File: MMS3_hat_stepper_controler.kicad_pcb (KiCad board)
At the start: 4 copper layers, 100 x 50 mm, 98 parts, among them J1 Chainbus in, J2 Chainbus Out, J3 Conn_01x04_Pin, J4 AMASS XT60 Male, J5 AMASS XT60 Female, J6 Encoder connector, J7 Motor connector, J8 Conn_01x03_Pin, SW1 SW_DIP_x04, U1 SN74CB3Q3384APW, U2 M24C64, U3 TMC5130A-TA, U4 AMS1117, U5 LM2596HVS-ADJRG

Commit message: generated production files
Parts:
- moved H7 9.00 mm to (88.0, 136.8)
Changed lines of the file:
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@@
 	(footprint "PCM_JLCPCB:Hole_Tooling_JLCPCB"
 		(layer "F.Cu")
-		(at 79 137)
+		(at 88 136.828427)
 		(property "Reference" "H7"
 			(at 0 -0.5 0)
@@
 			(polygon
 				(pts
-					(xy 78 136) (xy 80 136) (xy 80 138) (xy 78 138)
+					(xy 87 135.828427) (xy 89 135.828427) (xy 89 137.828427) (xy 87 137.828427)
 				)
 			)

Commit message: added version number
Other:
- board text added: "Version 1.0 Made by Wojciech Szafrański"
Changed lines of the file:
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@@
+		)
+	)
+	(gr_text "Version 1.0\nMade by\nWojciech Szafrański"
+		(at 102 131 -0)
+		(layer "B.SilkS")
+		(effects
+			(font
+				(size 1 1)
+				(thickness 0.2)
+				(bold yes)
+			)
+			(justify mirror)
 		)
 	)

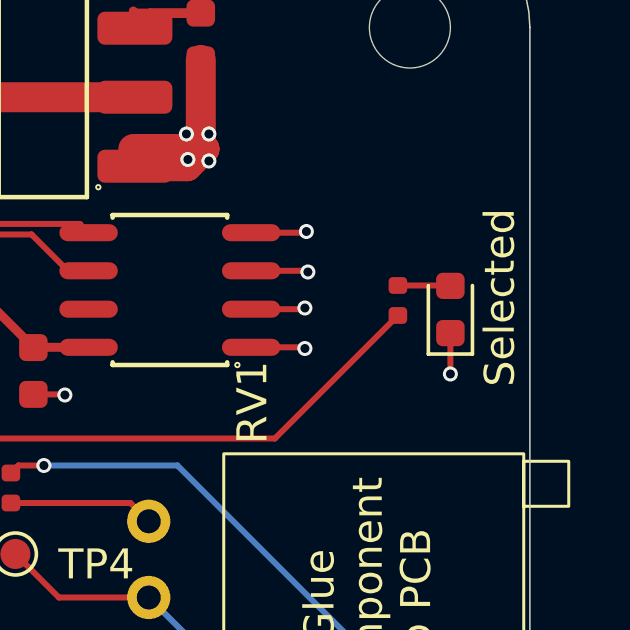
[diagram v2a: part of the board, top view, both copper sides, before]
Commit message: changed diode to JLCMANUFACTURING
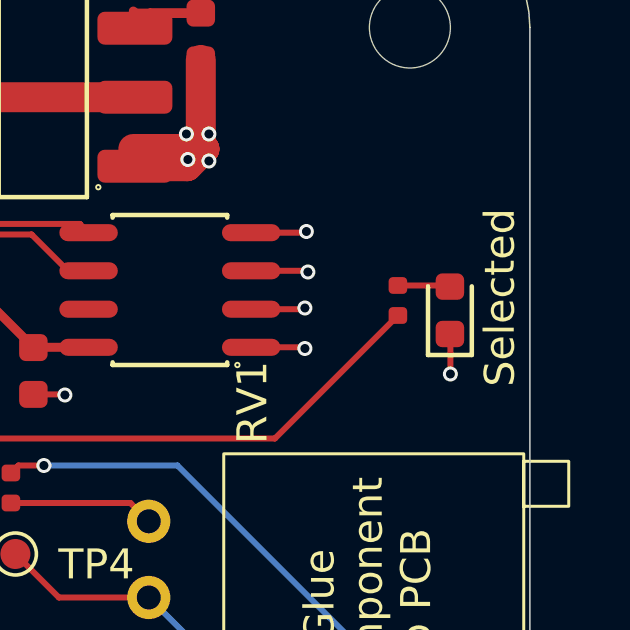
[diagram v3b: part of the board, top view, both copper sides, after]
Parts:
- removed D1: LED, LED_SMD:LED_0603_1608Metric
- added D7: Red, PCM_JLCPCB:D_0603, F.Cu at (175.3, 101.4)

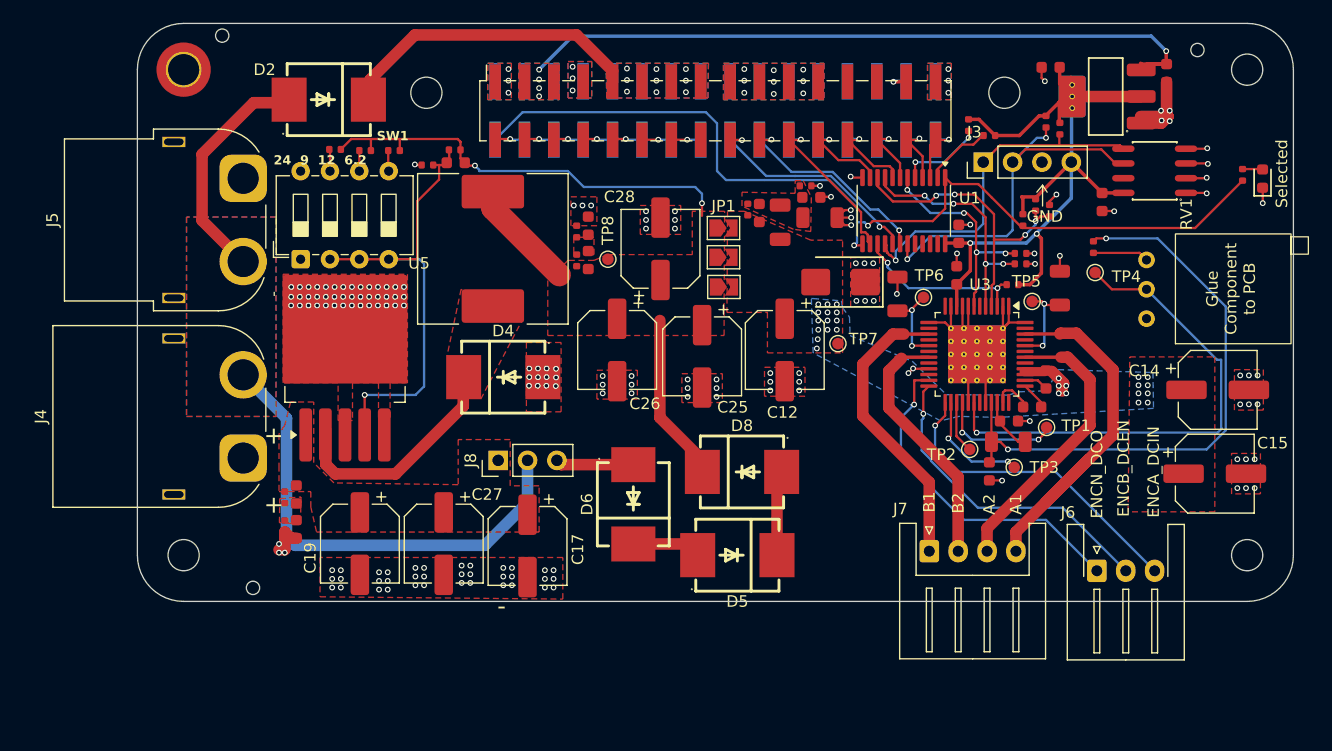
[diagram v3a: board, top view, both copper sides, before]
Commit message: moved XT60
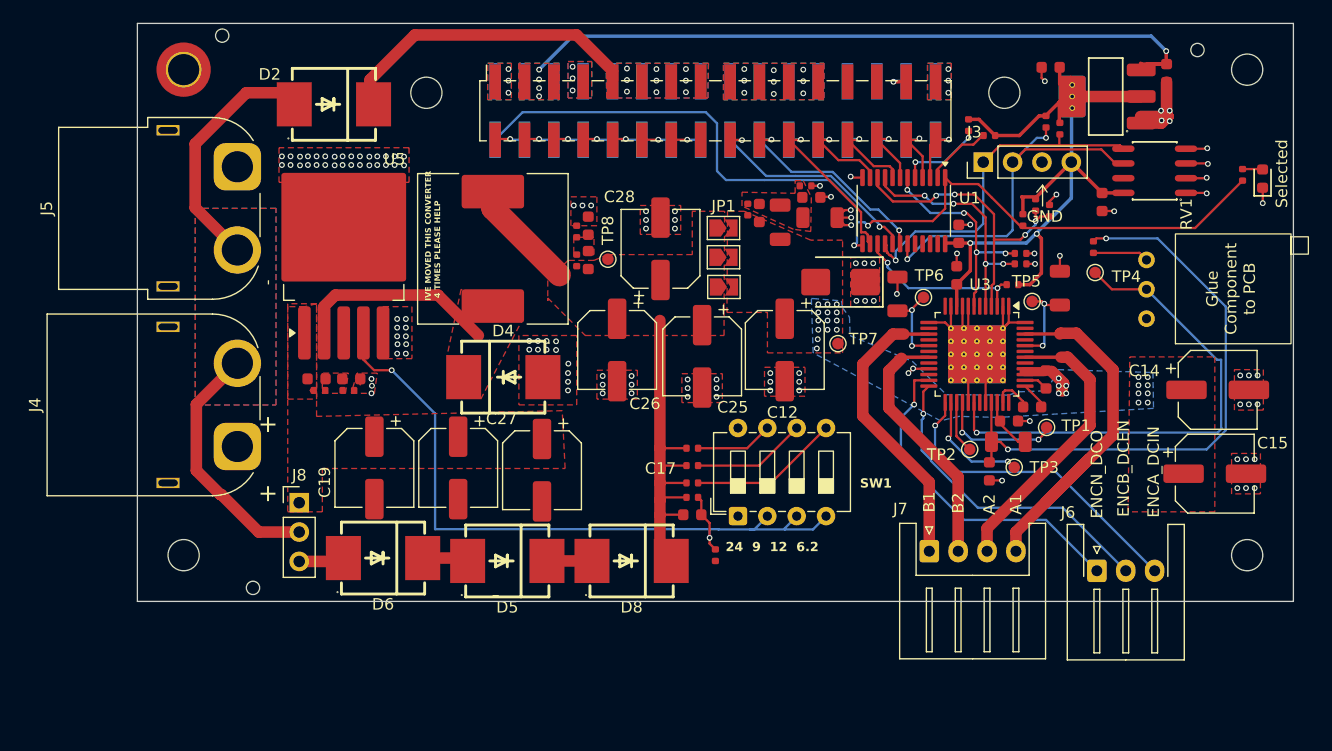
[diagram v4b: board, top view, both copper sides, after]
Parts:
- moved SW1 43.9 mm to (130.0, 130.6)
- moved R12 41.9 mm to (128.0, 134.0), turned to 90 degrees
- moved R14 40.3 mm to (126.0, 124.8), turned to 180 degrees
- moved R15 39.3 mm to (126.0, 126.2), turned to 180 degrees
- moved R16 38.6 mm to (126.0, 127.8), turned to 180 degrees
- moved C22 36.7 mm to (126.0, 130.5), turned to 180 degrees
- moved R13 36.4 mm to (126.0, 129.0), turned to 180 degrees
- moved D6 22.1 mm to (99.2, 134.2), turned to 180 degrees
- moved D5 19.9 mm to (110.0, 134.5)
- moved J8 17.6 mm to (92.0, 129.5), turned to 0 degrees
- moved C21 13.8 mm to (96.5, 118.8), turned to 0 degrees
- moved R11 13.0 mm to (96.2, 119.8), turned to 0 degrees
- moved D8 12.3 mm to (120.8, 134.5), turned to 180 degrees
- moved C20 10.2 mm to (93.5, 118.8), turned to 0 degrees
- moved R10 9.72 mm to (93.8, 119.8), turned to 0 degrees
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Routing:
- net Net-(U5-FB): track 41.8 -> 66.7 mm, vias 1 -> 2
- net U_reg: track 62.6 -> 42.2 mm, vias 2 -> 0
- net Vin: track 62.5 -> 42.9 mm
- net Net-(R16-Pad1): track 1.80 -> 13.0 mm
- net Net-(R15-Pad1): track 1.78 -> 9.88 mm
- net Net-(R14-Pad1): track 1.90 -> 6.72 mm
- net Net-(D5-K): track 7.37 -> 3.89 mm
- net GND: track 76.0 -> 72.6 mm, vias 183 -> 144
- net Net-(D6-A): track 6.97 -> 3.94 mm
- net Net-(D4-K): track 21.4 -> 18.8 mm
- net Net-(D5-A): track 5.97 -> 3.99 mm
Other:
- outline, holes or cut-outs redrawn
- board text added: "IVE MOVED THIS CONVERTER 4 TIMES PLEASE HELP"

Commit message: generated gerber
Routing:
- net GND: vias 144 -> 163
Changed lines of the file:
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@@
 		(at 99.25 134.25 180)
 		(property "Reference" "D6"
-			(at 0 -4 0)
+			(at 5.5 -2.95 0)
 			(layer "F.SilkS")
 			(effects
@@
 		(at 110 134.5 180)
 		(property "Reference" "D5"
-			(at 0 -4 0)
+			(at 5.5 -2.75 0)
 			(layer "F.SilkS")
 			(effects
@@
 		(tags "capacitor electrolytic")
 		(property "Reference" "C27"
-			(at -4.25 -3.75 180)
+			(at -3.95 -3.75 180)
 			(layer "F.SilkS")
 			(effects
@@
 		(tags "capacitor electrolytic")
 		(property "Reference" "C17"
-			(at -0.15 -10.25 0)
+			(at -3.65 -3.25 0)
 			(layer "F.SilkS")
 			(effects
@@
 		)
 		(fp_text user "+"
-			(at -4.08 2.6 90)
+			(at 7.1 2.6 90)
 			(layer "F.SilkS")
 			(effects
@@
 		(at 120.75 134.5 180)
 		(property "Reference" "D8"
-			(at 0 -4 0)
+			(at 5.25 -2.75 0)
 			(layer "F.SilkS")
 			(effects
@@
 		)
 		(fp_text user "+"
-			(at -22.3 2.6 90)
+			(at 0.15 3.55 90)
 			(layer "F.SilkS")
 			(effects
@@
 	)
 	(via
+		(at 114.25 130)
+		(size 0.5)
+		(drill 0.3)
+		(layers "F.Cu" "B.Cu")
+		(net 1)
+	)
+	(via
 		(at 90.5 99.5)
 		(size 0.5)
@@
 	)
 	(via
+		(at 99.75 128.25)
+		(size 0.5)
+		(drill 0.3)
+		(layers "F.Cu" "B.Cu")
+		(net 1)
+	)
+	(via
 		(at 141.65 108.75)
 		(size 0.5)
@@
 	)
 	(via
+		(at 114.25 128.5)
+		(size 0.5)
+		(drill 0.3)
+		(layers "F.Cu" "B.Cu")
+		(net 1)
+	)
+	(via
 		(at 115.65 93.8)
 		(size 0.5)
@@
 	)
 	(via
+		(at 99.75 129.75)
+		(size 0.5)
+		(drill 0.3)
+		(layers "F.Cu" "B.Cu")
+		(net 1)
+	)
+	(via
+		(at 104.5 129)
+		(size 0.5)
+		(drill 0.3)
+		(layers "F.Cu" "B.Cu")
+		(net 1)
+	)
+	(via
 		(at 95.75 99.5)
 		(size 0.5)
@@
 	)
 	(via
+		(at 111.75 130)
+		(size 0.5)
+		(drill 0.3)
+		(layers "F.Cu" "B.Cu")
+		(net 1)
+	)
+	(via
+		(at 99.75 129)
+		(size 0.5)
+		(drill 0.3)
+		(layers "F.Cu" "B.Cu")
+		(net 1)
+	)
+	(via
 		(at 115.277248 117.43255)
 		(size 0.5)
@@
 	)
 	(via
+		(at 97.25 129.75)
+		(size 0.5)
+		(drill 0.3)
+		(layers "F.Cu" "B.Cu")
+		(net 1)
+	)
+	(via
 		(at 173.4 120.95)
 		(size 0.5)
@@
 	)
 	(via
+		(at 111.75 129.25)
+		(size 0.5)
+		(drill 0.3)
+		(layers "F.Cu" "B.Cu")
+		(net 1)
+	)
+	(via
 		(at 155.65 108.8)
 		(size 0.5)
@@
 	)
 	(via
+		(at 114.25 129.25)
+		(size 0.5)
+		(drill 0.3)
+		(layers "F.Cu" "B.Cu")
+		(net 1)
+	)
+	(via
+		(at 104.5 129.75)
+		(size 0.5)
+		(drill 0.3)
+		(layers "F.Cu" "B.Cu")
+		(net 1)
+	)
+	(via
 		(at 166.6 96.4)
 		(size 0.5)
@@
 	)
 	(via
+		(at 104.5 128.25)
+		(size 0.5)
+		(drill 0.3)
+		(layers "F.Cu" "B.Cu")
+		(net 1)
+	)
+	(via
 		(at 174.65 125.7)
 		(size 0.5)
@@
 	)
 	(via
+		(at 95.75 113.75)
+		(size 0.5)
+		(drill 0.3)
+		(layers "F.Cu" "B.Cu")
+		(net 1)
+	)
+	(via
 		(at 100.472752 113.56745)
 		(size 0.5)
@@
 	)
 	(via
+		(at 97.25 129)
+		(size 0.5)
+		(drill 0.3)
+		(layers "F.Cu" "B.Cu")
+		(net 1)
+	)
+	(via
 		(at 95.75 100.25)
 		(size 0.5)
@@
 	)
 	(via
+		(at 97.25 128.25)
+		(size 0.5)
+		(drill 0.3)
+		(layers "F.Cu" "B.Cu")
+		(net 1)
+	)
+	(via
 		(at 100.25 99.5)
 		(size 0.5)
@@
 	)
 	(via
+		(at 107 129.75)
+		(size 0.5)
+		(drill 0.3)
+		(layers "F.Cu" "B.Cu")
+		(net 1)
+	)
+	(via
 		(at 135.25 119)
 		(size 0.5)
@@
 	)
 	(via
+		(at 107 129)
+		(size 0.5)
+		(drill 0.3)
+		(layers "F.Cu" "B.Cu")
+		(net 1)
+	)
+	(via
 		(at 140.9 108.75)
 		(size 0.5)
@@
 	)
 	(via
+		(at 111.75 128.5)
+		(size 0.5)
+		(drill 0.3)
+		(layers "F.Cu" "B.Cu")
+		(net 1)
+	)
+	(via
 		(at 114.21745 116.25)
 		(size 0.5)
@@
 	)
 	(via
+		(at 107 128.25)
+		(size 0.5)
+		(drill 0.3)
+		(layers "F.Cu" "B.Cu")
+		(net 1)
+	)
+	(via
 		(at 97.25 99.5)
 		(size 0.5)
@@
 	)
 	(zone
+		(net 1)
+		(net_name "GND")
+		(layer "F.Cu")
+		(hatch edge 0.5)
+		(priority 7)
+		(connect_pads yes
+			(clearance 0.2)
+		)
+		(min_thickness 0.25)
+		(filled_areas_thickness no)
+		(fill yes
+			(thermal_gap 0.5)
+			(thermal_bridge_width 0.5)
+		)
+		(polygon
+			(pts
+				(xy 100.25 130.25) (xy 96.75 130.25) (xy 96.75 127.75) (xy 100.25 127.75)
+			)
+		)
+	)
+	(zone
 		(net 12)
 		(net_name "Net-(J8-Pin_1)")
@@
 			)
 		)
+	)
+	(zone
+		(net 1)
+		(net_name "GND")
+		(layer "F.Cu")
+		(hatch edge 0.5)
+		(priority 7)
+		(connect_pads yes
+			(clearance 0.2)
+		)
+		(min_thickness 0.25)
+		(filled_areas_thickness no)
+		(fill yes
+			(thermal_gap 0.5)
+			(thermal_bridge_width 0.5)
+		)
+		(polygon
+			(pts
+				(xy 114.75 130.5) (xy 111.25 130.5) (xy 111.25 128) (xy 114.75 128)
+			)
+		)
+	)
+	(zone
+		(net 1)
+		(net_name "GND")
+		(layer "F.Cu")
+		(hatch edge 0.5)
+		(priority 7)
+		(connect_pads yes
+			(clearance 0.2)
+		)
+		(min_thickness 0.25)
+		(filled_areas_thickness no)
+		(fill yes
+			(thermal_gap 0.5)
+			(thermal_bridge_width 0.5)
+		)
+		(polygon
+			(pts
+				(xy 107.5 130.25) (xy 104 130.25) (xy 104 127.75) (xy 107.5 127.75)
+			)
+		)

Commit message: ... I forgot to move the converter.
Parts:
- moved H1 42.0 mm to (82.0, 134.0)
- moved H3 42.0 mm to (82.0, 92.0)
- moved J4 30.1 mm to (116.3, 129.6), turned to 180 degrees
- moved D2 29.9 mm to (81.2, 121.5), turned to -90 degrees
- moved J5 29.8 mm to (92.0, 129.8), turned to 180 degrees
- moved C17 27.3 mm to (88.3, 115.0), turned to 180 degrees
- moved D6 20.5 mm to (117.0, 124.0)
- moved C27 17.8 mm to (88.2, 123.4)
- moved R12 15.4 mm to (140.2, 124.8), turned to 0 degrees
- moved D5 15.1 mm to (124.5, 130.2), turned to 90 degrees
- moved C22 14.7 mm to (137.2, 121.0)
- moved SW1 13.2 mm to (142.2, 135.5), turned to 180 degrees
- moved R13 12.7 mm to (136.8, 122.2)
- moved J8 12.5 mm to (103.5, 124.5), turned to 90 degrees
- moved R14 12.0 mm to (138.0, 124.5), turned to 90 degrees
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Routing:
- net BRD_VIN: track 25.9 -> 74.0 mm
- net GND: track 72.6 -> 93.3 mm, vias 163 -> 149
- net Net-(U5-FB): track 66.7 -> 83.2 mm
- net U_reg: track 42.2 -> 25.8 mm
- net Vin: track 42.9 -> 29.4 mm
- net Net-(D4-K): track 18.8 -> 5.72 mm
- net Net-(R16-Pad1): track 13.0 -> 2.93 mm
- net Net-(R15-Pad1): track 9.88 -> 6.09 mm
- net Net-(R14-Pad1): track 6.72 -> 9.36 mm
- net Net-(D5-K): track 3.89 -> 6.02 mm
- net Net-(D6-A): track 3.94 -> 5.24 mm
- net Net-(D5-A): track 3.99 -> 5.24 mm
- removed copper zone on B.Cu, net Vin

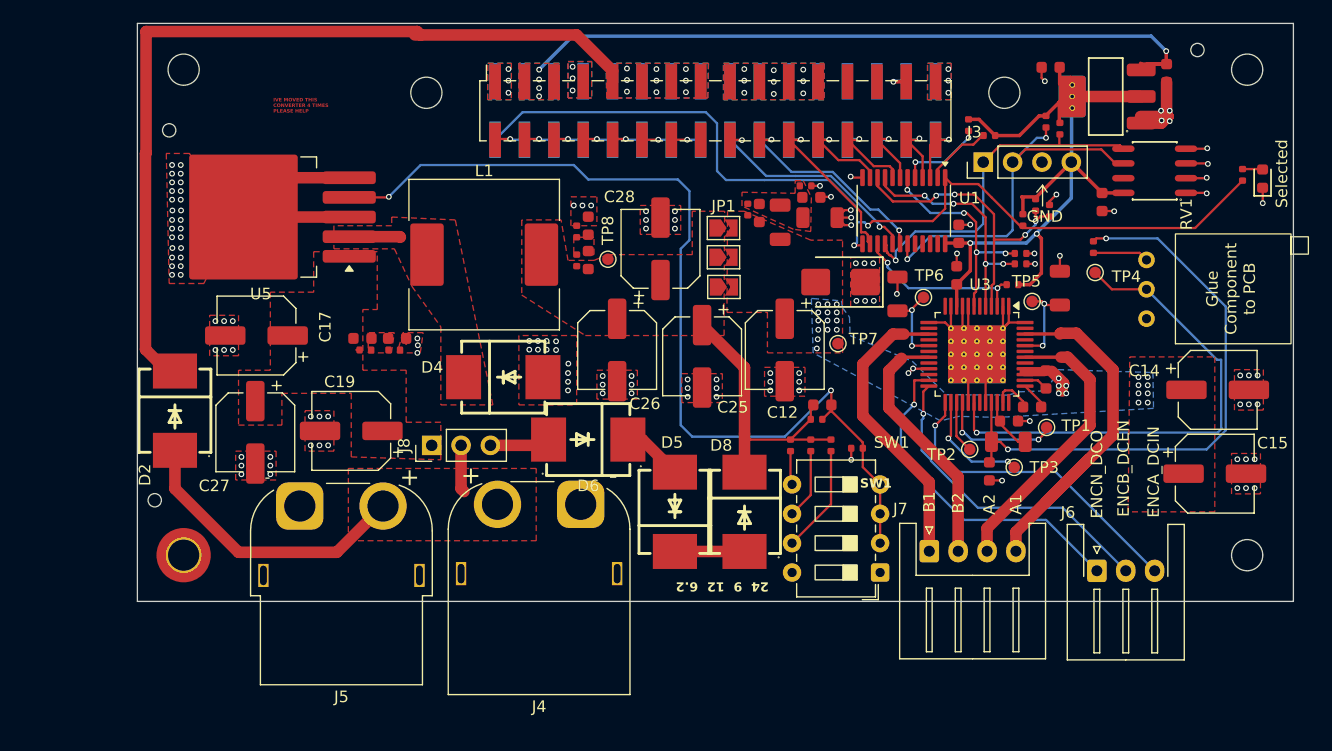
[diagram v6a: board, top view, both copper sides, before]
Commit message: moved the converter, to the long side this time
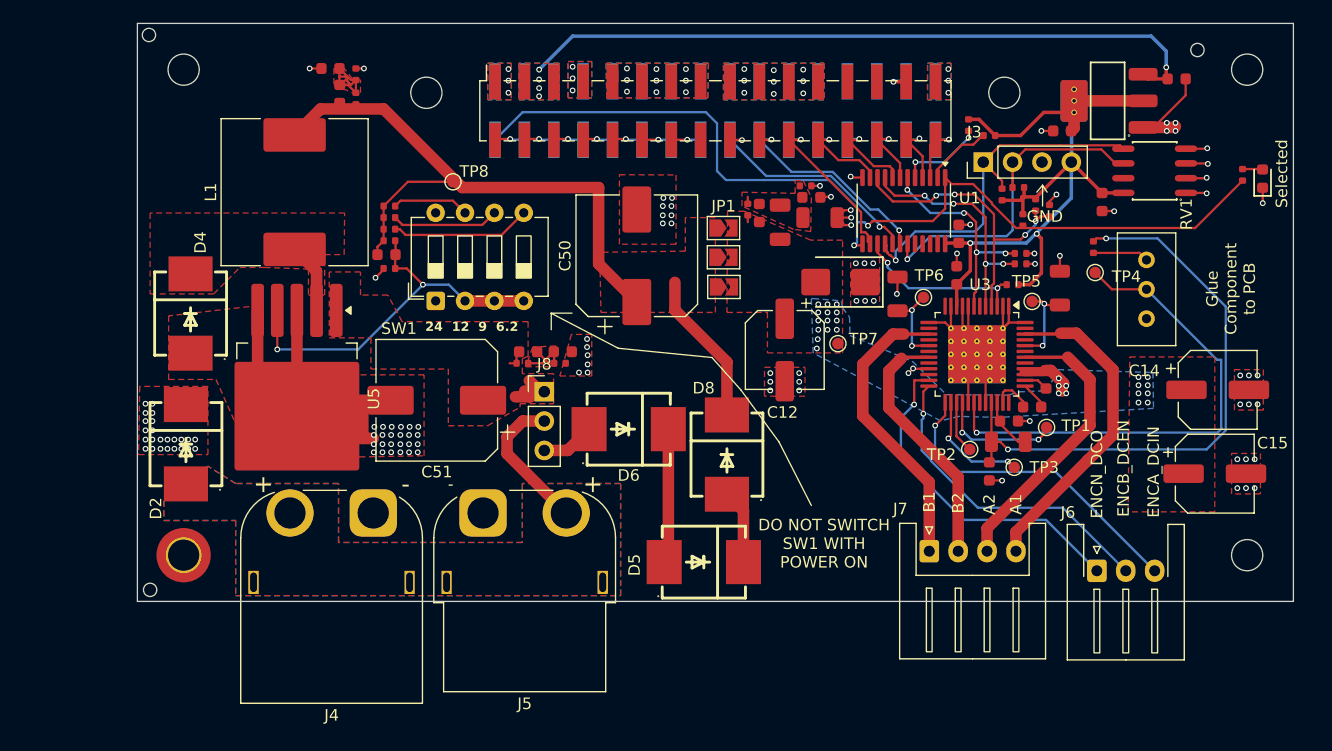
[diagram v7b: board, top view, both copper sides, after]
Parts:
- removed C17, C19, C25, C26, C27, C28: 47u, Capacitor_SMD:CP_Elec_6.3x7.7
- added C50: 100uF, Capacitor_SMD:CP_Elec_10x10, F.Cu at (121.2, 108.1)
- added C51: 100uF, Capacitor_SMD:CP_Elec_10x10, F.Cu at (103.9, 120.6)
- moved SW1 45.1 mm to (103.8, 112.0), turned to 90 degrees
- moved R14 43.4 mm to (99.8, 103.8), turned to 180 degrees
- moved R12 43.3 mm to (99.8, 109.2)
- moved R15 41.4 mm to (99.8, 104.8), turned to 180 degrees
- moved R13 40.1 mm to (99.8, 106.8)
- moved C22 39.9 mm to (99.5, 108.0)
- moved R16 39.4 mm to (99.8, 105.8), turned to 180 degrees
- moved D4 27.6 mm to (82.6, 113.1), turned to -90 degrees
- moved C24 26.1 mm to (94.7, 91.9), turned to 180 degrees
- moved C23 25.9 mm to (95.5, 94.1)
- moved R17 23.7 mm to (96.9, 94.5)
- moved R18 23.4 mm to (96.9, 92.4)
- moved J4 18.0 mm to (98.4, 130.3)
- moved L1 17.3 mm to (91.6, 102.6), turned to 90 degrees
- moved U5 16.0 mm to (91.8, 120.5), turned to -90 degrees
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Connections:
- net Net-(D4-K) renamed /Buck Regulator/sw
- net Net-(J8-Pin_1) renamed /Buck Regulator/sw-vin
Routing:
- net Net-(U5-FB): track 83.2 -> 33.2 mm
- net U_reg: track 25.8 -> 65.9 mm
- net GND: track 93.3 -> 114.2 mm, vias 149 -> 109
- net Vin: track 29.4 -> 12.5 mm
- net Net-(C23-Pad2): track 0.00 -> 10.1 mm
- net Net-(R16-Pad1): track 2.93 -> 12.1 mm
- net /Buck Regulator/sw-vin: track 0.49 -> 7.80 mm
- net Net-(D5-A): track 5.24 -> 11.6 mm
- net BRD_VIN: track 74.0 -> 80.0 mm, vias 9 -> 33
- net Net-(C20-Pad2): track 0.00 -> 5.53 mm
- net /Stepper controller/OA1: track 33.9 -> 28.7 mm
- net Net-(R15-Pad1): track 6.09 -> 9.28 mm
- net Net-(R14-Pad1): track 9.36 -> 6.67 mm
- net /Bus_switch/Chainbus.SCL: track 32.6 -> 30.1 mm, vias 2 -> 1
- net /Bus_switch/Chainbus.SDA: track 30.3 -> 32.4 mm
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- added copper zone on In1.Cu, net BRD_VIN
- added copper zone on In2.Cu, net BRD_VIN
- added copper zone on B.Cu, net Vin
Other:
- board text added: "24 12 9 6.2"
- board text added: "DO NOT SWITCH SW1 WITH POWER ON"
- board text removed: "24 9 12 6.2"
- board text removed: "IVE MOVED THIS CONVERTER 4 TIMES PLEASE HELP"
- board text removed: "SW1"
